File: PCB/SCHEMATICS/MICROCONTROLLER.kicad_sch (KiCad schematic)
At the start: 29 parts, among them IC1 CP2102-GMR, U6 C6482, U7 C6482

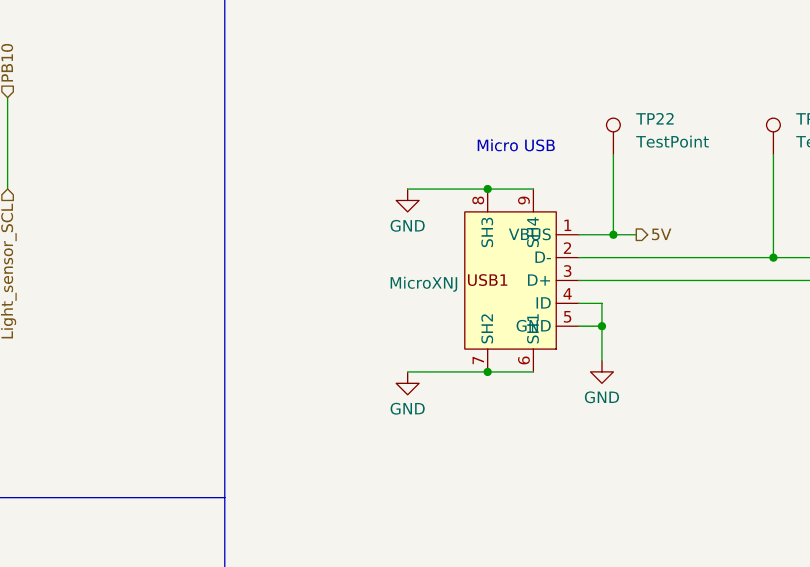
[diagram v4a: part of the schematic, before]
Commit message: Fixed ercs
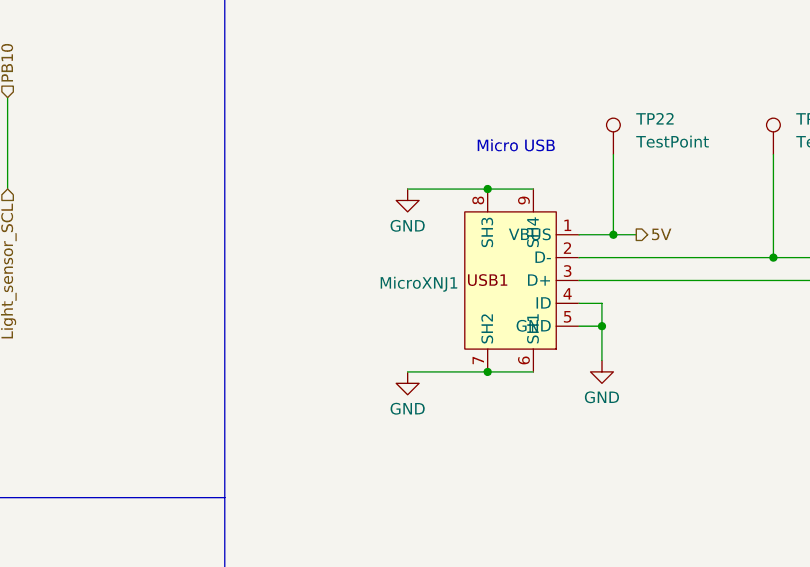
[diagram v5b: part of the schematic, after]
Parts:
- TP22, TP23, TP24, TP25, TP26, TP27, TP32, TP33, TP34, TP35: footprint (none) -> TestPoint:TestPoint_Bridge_Pitch2.0mm_Drill0.7mm
- renumbered MicroXNJ to MicroXNJ1
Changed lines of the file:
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@@
       (effects (font (size 1.27 1.27)) (justify left))
     )
-    (property "Footprint" "" (at 158.75 39.37 0)
+    (property "Footprint" "TestPoint:TestPoint_Bridge_Pitch2.0mm_Drill0.7mm" (at 158.75 39.37 0)
       (effects (font (size 1.27 1.27)) hide)
     )
@@
       (effects (font (size 1.27 1.27)) (justify left))
     )
-    (property "Footprint" "" (at 140.97 39.37 0)
+    (property "Footprint" "TestPoint:TestPoint_Bridge_Pitch2.0mm_Drill0.7mm" (at 140.97 39.37 0)
       (effects (font (size 1.27 1.27)) hide)
     )
@@
       (effects (font (size 1.27 1.27)) (justify left))
     )
-    (property "Footprint" "" (at 52.07 168.91 0)
+    (property "Footprint" "TestPoint:TestPoint_Bridge_Pitch2.0mm_Drill0.7mm" (at 52.07 168.91 0)
       (effects (font (size 1.27 1.27)) hide)
     )
@@
       (effects (font (size 1.27 1.27)) (justify left))
     )
-    (property "Footprint" "" (at 52.07 171.45 0)
+    (property "Footprint" "TestPoint:TestPoint_Bridge_Pitch2.0mm_Drill0.7mm" (at 52.07 171.45 0)
       (effects (font (size 1.27 1.27)) hide)
     )
@@
       (effects (font (size 1.27 1.27)) (justify left))
     )
-    (property "Footprint" "" (at 175.26 39.37 0)
+    (property "Footprint" "TestPoint:TestPoint_Bridge_Pitch2.0mm_Drill0.7mm" (at 175.26 39.37 0)
       (effects (font (size 1.27 1.27)) hide)
     )
@@
       (effects (font (size 1.27 1.27)) (justify left))
     )
-    (property "Footprint" "" (at 52.07 173.99 0)
+    (property "Footprint" "TestPoint:TestPoint_Bridge_Pitch2.0mm_Drill0.7mm" (at 52.07 173.99 0)
       (effects (font (size 1.27 1.27)) hide)
     )
@@
       (effects (font (size 1.27 1.27)) (justify left))
     )
-    (property "Footprint" "" (at 46.99 158.75 0)
+    (property "Footprint" "TestPoint:TestPoint_Bridge_Pitch2.0mm_Drill0.7mm" (at 46.99 158.75 0)
       (effects (font (size 1.27 1.27)) hide)
     )
@@
   (symbol (lib_id "DEBUGGER:Micro_usb") (at 124.46 63.5 180) (unit 1)
     (in_bom yes) (on_board yes) (dnp no) (fields_autoplaced)
-    (property "Reference" "MicroXNJ" (at 118.7037 53.6568 0)
+    (property "Reference" "MicroXNJ1" (at 118.7037 53.6568 0)
       (effects (font (size 1.27 1.27)) (justify left))
     )
@@
       (project "SCHEMATICS"
         (path "/c9ca3a5c-30cb-4dce-b611-3270b9f3284b/f1cf3ff5-1ffc-45ee-bf83-2ece91c9ccf0"
-          (reference "MicroXNJ") (unit 1)
+          (reference "MicroXNJ1") (unit 1)
         )
       )
@@
       (effects (font (size 1.27 1.27)) (justify left))
     )
-    (property "Footprint" "" (at 68.58 107.95 0)
+    (property "Footprint" "TestPoint:TestPoint_Bridge_Pitch2.0mm_Drill0.7mm" (at 68.58 107.95 0)
       (effects (font (size 1.27 1.27)) hide)
     )
@@
       (effects (font (size 1.27 1.27)) (justify left))
     )
-    (property "Footprint" "" (at 76.2 107.95 0)
+    (property "Footprint" "TestPoint:TestPoint_Bridge_Pitch2.0mm_Drill0.7mm" (at 76.2 107.95 0)
       (effects (font (size 1.27 1.27)) hide)
     )
@@
       (effects (font (size 1.27 1.27)) (justify left))
     )
-    (property "Footprint" "" (at 59.69 96.52 0)
-      (effects (font (size 1.27 1.27)) hide)
-    )
+    (property "Footprint" "TestPoint:TestPoint_Bridge_Pitch2.0mm_Drill0.7mm" (at 59.69 96.52 0)
+      (effects (font (size 1.27 1.27)) hide)
+    )

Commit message: Fixing ERCs
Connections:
- net D+: now also C6.2; no longer C6.2
- net D-: now also C6.2; no longer C6.2

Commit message: Started PCB design
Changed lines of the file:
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@@
+    (stroke (width 0) (type default))
+  )
+  (wire (pts (xy 22.225 83.82) (xy 22.225 89.535))
     (stroke (width 0) (type default))
   )
@@
   )
   (hierarchical_label "3V3" (shape input) (at 229.87 54.61 180) (fields_autoplaced)
+    (effects (font (size 1.27 1.27)) (justify right))
+  )
+  (hierarchical_label "3V3" (shape input) (at 22.225 89.535 270) (fields_autoplaced)
     (effects (font (size 1.27 1.27)) (justify right))
   )
@@
         )
       )
+    )
+  )
+  (symbol (lib_id "power:PWR_FLAG") (at 22.225 83.82 0) (unit 1)
+    (in_bom yes) (on_board yes) (dnp no) (fields_autoplaced)
+    (property "Reference" "#FLG02" (at 22.225 81.915 0)
+      (effects (font (size 1.27 1.27)) hide)
+    )
+    (property "Value" "PWR_FLAG" (at 22.225 80.645 0)
+      (effects (font (size 1.27 1.27)))
+    )
+    (property "Footprint" "" (at 22.225 83.82 0)
+      (effects (font (size 1.27 1.27)) hide)
+    )
+    (property "Datasheet" "~" (at 22.225 83.82 0)
+      (effects (font (size 1.27 1.27)) hide)
+    )
+    (pin "1")
+    (instances
+      (project "SCHEMATICS"
+        (path "/c9ca3a5c-30cb-4dce-b611-3270b9f3284b/c574ee02-103d-4bad-a8c0-5ec1707f609e"
+          (reference "#FLG02") (unit 1)
+        )
+        (path "/c9ca3a5c-30cb-4dce-b611-3270b9f3284b/f1cf3ff5-1ffc-45ee-bf83-2ece91c9ccf0"
+          (reference "#FLG07") (unit 1)
+        )
+      )
